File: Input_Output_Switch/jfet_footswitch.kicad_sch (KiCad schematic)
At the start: 48 parts, among them Q1 MMBF4393LT1G, Q2 PZT2222A, Q3 MMBF4393LT1G, Q4 PZT2222A, SW1 SW_Push, U2 TL072

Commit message: Final version 1.0 ordered
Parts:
- removed Q2, Q4: PZT2222A, Package_TO_SOT_SMD:SOT-23, symbol Transistor_BJT:PZT2222A
- added Q2, Q4: 2N4401D75ZCT-ND, Package_TO_SOT_THT:TO-92_Inline_Wide, symbol Device:Q_NPN_EBC
- C10, C11, C12, C13, C14, C15, C16: footprint Capacitor_SMD:C_0805_2012Metric -> Capacitor_SMD:C_0603_1608Metric_Pad1.08x0.95mm_HandSolder
- TP1, TP13, TP14, TP2, TP3, TP6, TPG3, TPG4: now left out of the parts list
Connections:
- net GNDA: now also Q2.1 (E), Q4.1 (E)
- net at C12.2, C14.1, R16.1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: now also Q4.2 (B)
- net at C15.1, R18.1, R20.1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: now also Q4.3 (C)
- net at C13.2, C15.2, R15.2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: now also Q2.2 (B)
- net at C12.1, D4.1 (K), R13.1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: now also Q2.3 (C)
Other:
- title: (none) -> EQ8-Main-Board

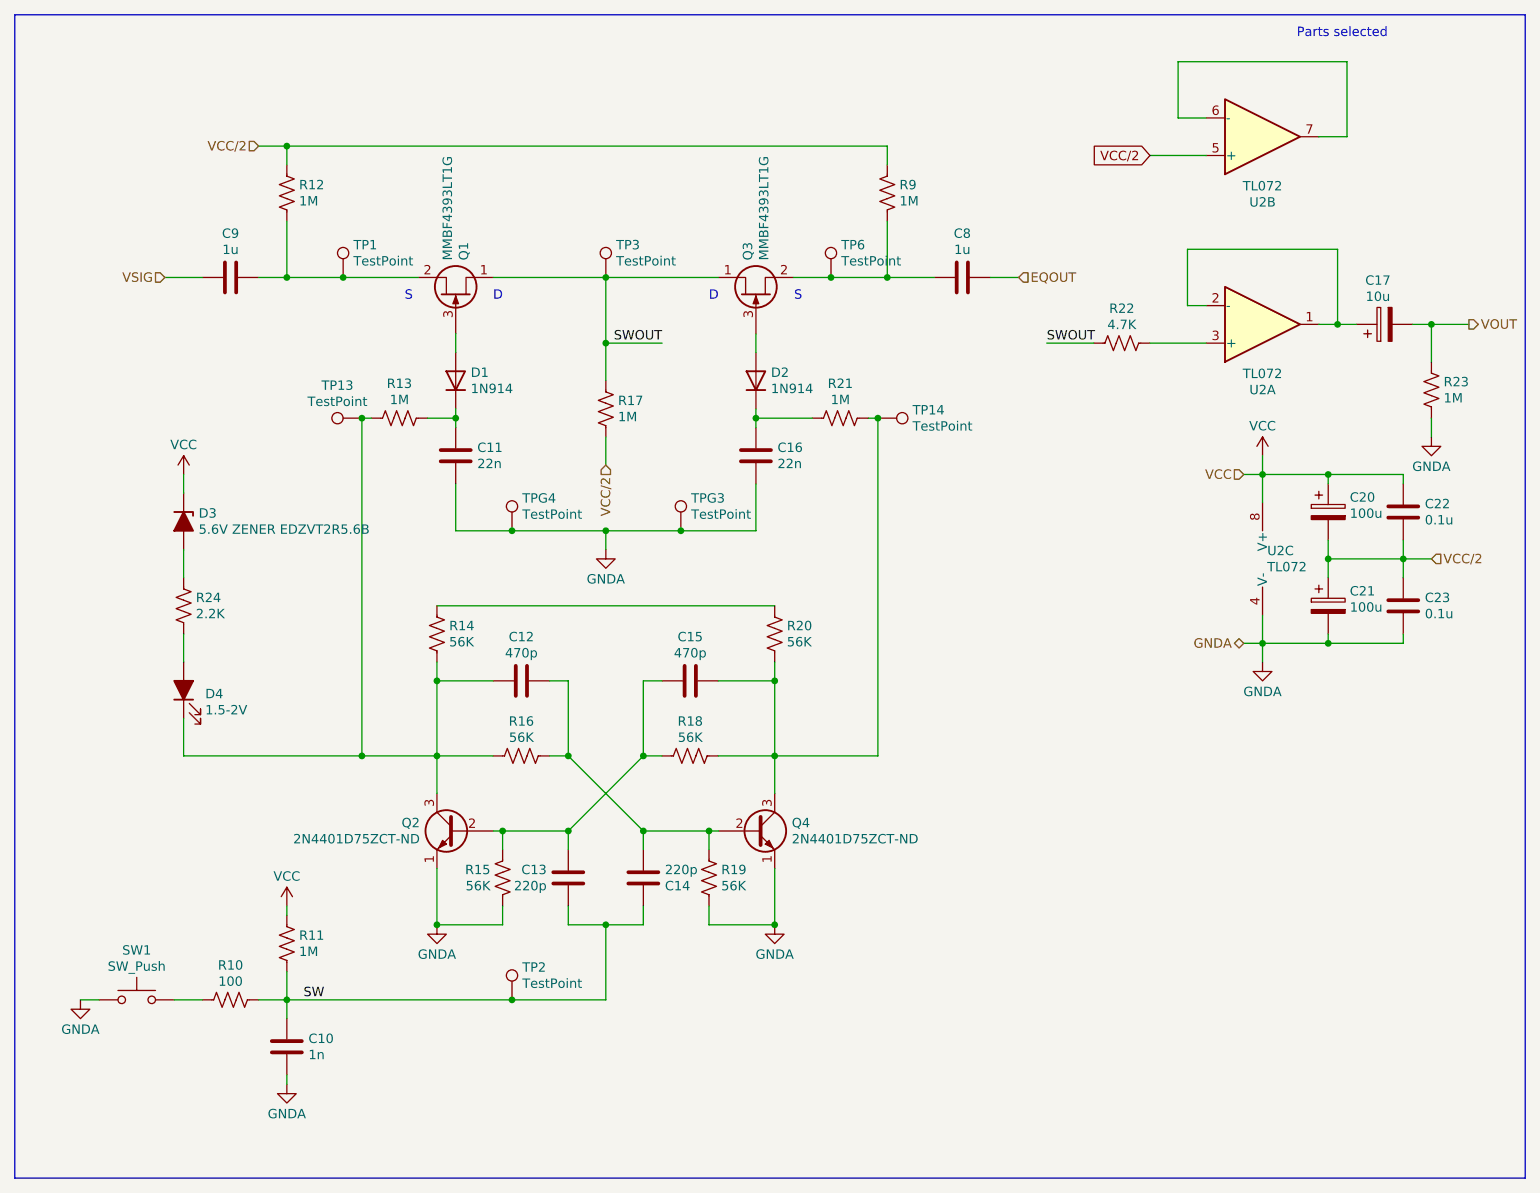
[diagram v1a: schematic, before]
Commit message: Fix bypass resistor, add missing Vcc. Move to Kicad-9
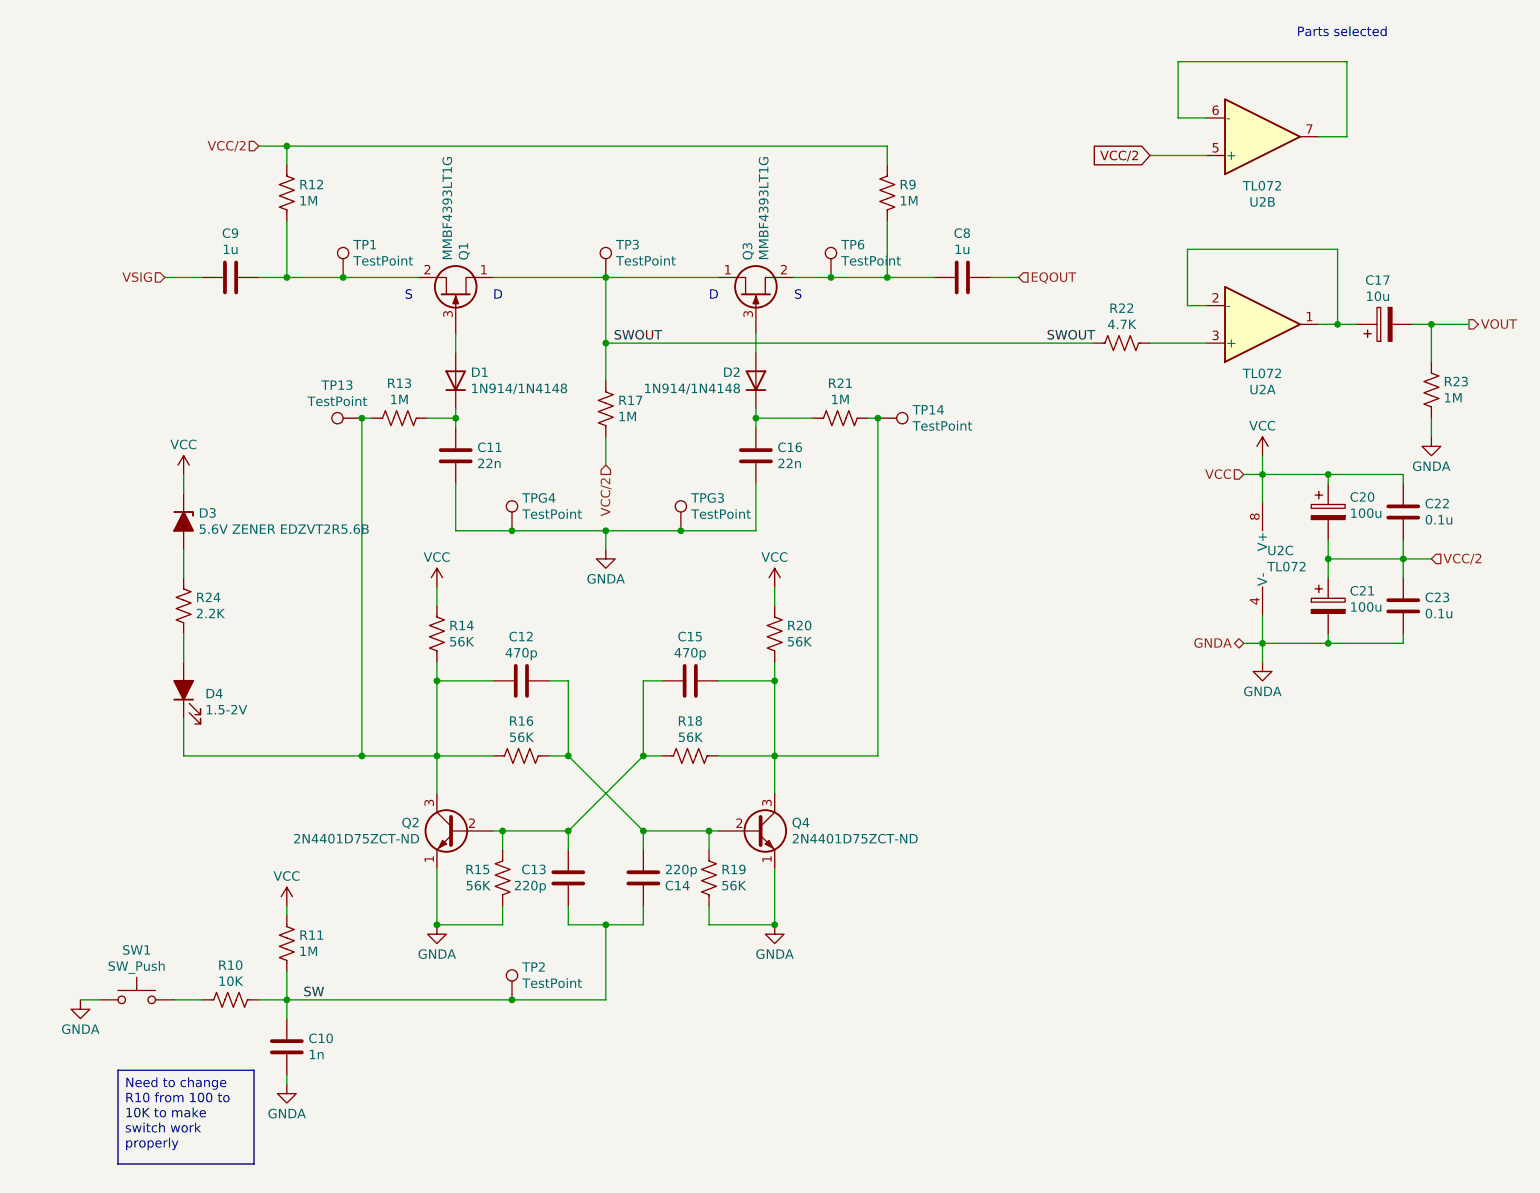
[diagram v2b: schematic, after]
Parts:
- D1, D2: value 1N914 -> 1N914/1N4148
- R10: value 100 -> 10K
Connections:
- net VCC: now also R14.2, R20.2
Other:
- moved on the sheet: D2
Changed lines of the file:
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@@
 (kicad_sch
-	(version 20231120)
+	(version 20250114)
 	(generator "eeschema")
-	(generator_version "8.0")
+	(generator_version "9.0")
 	(paper "A4")
 	(title_block
 		(title "EQ8-Main-Board")
-		(date "2024-11-23")
-		(rev "1.0")
+		(date "2025-07-25")
+		(rev "v1.1")
+	)
+	(text "D"
+		(exclude_from_sim no)
+		(at 125.095 52.07 0)
+		(effects
+			(font
+				(size 1.27 1.27)
+			)
+		)
+	)
+	(text "D"
+		(exclude_from_sim no)
+		(at 154.305 52.07 0)
+		(effects
+			(font
+				(size 1.27 1.27)
+			)
+		)
+	)
+	(text "S"
+		(exclude_from_sim no)
+		(at 165.735 52.07 0)
+		(effects
+			(font
+				(size 1.27 1.27)
+			)
+		)
+	)
+	(text "Parts selected"
+		(exclude_from_sim no)
+		(at 239.395 16.51 0)
+		(effects
+			(font
+				(size 1.27 1.27)
+			)
+		)
+	)
+	(text "S"
+		(exclude_from_sim no)
+		(at 113.03 52.07 0)
+		(effects
+			(font
+				(size 1.27 1.27)
+			)
+		)
+	)
+	(text_box "Need to change R10 from 100 to 10K to make switch work properly"
+		(exclude_from_sim no)
+		(at 73.66 156.845 0)
+		(size 18.415 12.7)
+		(margins 0.9525 0.9525 0.9525 0.9525)
+		(stroke
+			(width 0)
+			(type default)
+		)
+		(fill
+			(type none)
+		)
+		(effects
+			(font
+				(size 1.27 1.27)
+			)
+			(justify left top)
+		)
 	)
 	(junction
@@
 	(wire
 		(pts
-			(xy 116.84 93.98) (xy 162.56 93.98)
-		)
-		(stroke
-			(width 0)
-			(type default)
-		)
-	)
-	(wire
-		(pts
 			(xy 119.38 57.15) (xy 119.38 59.69)
 		)
@@
 	(wire
 		(pts
-			(xy 199.39 58.42) (xy 205.74 58.42)
-		)
-		(stroke
-			(width 0)
-			(type default)
-		)
-	)
-	(wire
-		(pts
 			(xy 81.28 147.32) (xy 85.09 147.32)
 		)
@@
 	(wire
 		(pts
-			(xy 139.7 58.42) (xy 147.32 58.42)
+			(xy 139.7 58.42) (xy 205.74 58.42)
 		)
 		(stroke
@@
 	(wire
 		(pts
+			(xy 162.56 91.44) (xy 162.56 93.98)
+		)
+		(stroke
+			(width 0)
+			(type default)
+		)
+	)
+	(wire
+		(pts
 			(xy 96.52 41.91) (xy 96.52 49.53)
 		)
@@
 	(wire
 		(pts
-			(xy 139.7 83.82) (xy 149.86 83.82)
+			(xy 116.84 91.44) (xy 116.84 93.98)
 		)
 		(stroke
@@
 	(wire
 		(pts
-			(xy 162.56 101.6) (xy 162.56 104.14)
+			(xy 139.7 83.82) (xy 149.86 83.82)
 		)
 		(stroke
@@
 	(wire
 		(pts
-			(xy 160.02 83.82) (xy 160.02 77.47)
+			(xy 162.56 101.6) (xy 162.56 104.14)
 		)
 		(stroke
@@
 		)
 	)
-	(rectangle
-		(start 59.69 13.97)
-		(end 264.16 171.45)
+	(wire
+		(pts
+			(xy 160.02 83.82) (xy 160.02 77.47)
+		)
 		(stroke
 			(width 0)
 			(type default)
 		)
-		(fill
-			(type none)
-		)
-	)
-	(text "D"
-		(exclude_from_sim no)
-		(at 125.095 52.07 0)
-		(effects
-			(font
-				(size 1.27 1.27)
-			)
-		)
-	)
-	(text "D"
-		(exclude_from_sim no)
-		(at 154.305 52.07 0)
-		(effects
-			(font
-				(size 1.27 1.27)
-			)
-		)
-	)
-	(text "S"
-		(exclude_from_sim no)
-		(at 165.735 52.07 0)
-		(effects
-			(font
-				(size 1.27 1.27)
-			)
-		)
-	)
-	(text "Parts selected"
-		(exclude_from_sim no)
-		(at 239.395 16.51 0)
-		(effects
-			(font
-				(size 1.27 1.27)
-			)
-		)
-	)
-	(text "S"
-		(exclude_from_sim no)
-		(at 113.03 52.07 0)
-		(effects
-			(font
-				(size 1.27 1.27)
-			)
-		)
 	)
 	(label "SW"
 		(at 101.6 147.32 180)
-		(fields_autoplaced yes)
 		(effects
 			(font
@@
 	(label "SWOUT"
 		(at 147.32 58.42 180)
-		(fields_autoplaced yes)
 		(effects
 			(font
@@
 	(label "SWOUT"
 		(at 199.39 58.42 0)
-		(fields_autoplaced yes)
 		(effects
 			(font
@@
 		(shape input)
 		(at 139.7 74.93 270)
-		(fields_autoplaced yes)
 		(effects
 			(font
@@
 		(shape input)
 		(at 80.01 49.53 180)
-		(fields_autoplaced yes)
 		(effects
 			(font
@@
 		(shape input)
 		(at 226.06 76.2 180)
-		(fields_autoplaced yes)
 		(effects
 			(font
@@
 		(shape input)
 		(at 195.58 49.53 0)
-		(fields_autoplaced yes)
 		(effects
 			(font
@@
 		(shape output)
 		(at 256.54 55.88 0)
-		(fields_autoplaced yes)
 		(effects
 			(font
@@
 		(shape input)
 		(at 92.71 31.75 180)
-		(fields_autoplaced yes)
 		(effects
 			(font
@@
 		(shape bidirectional)
 		(at 226.06 99.06 180)
-		(fields_autoplaced yes)
 		(effects
 			(font
@@
 		(shape input)
 		(at 251.46 87.63 0)
-		(fields_autoplaced yes)
 		(effects
 			(font
@@
 		(fields_autoplaced yes)
 		(property "Reference" "R10"
-			(at 88.9 142.6417 90)
+			(at 88.9 142.6716 90)
 			(effects
 				(font
@@
 			)
 		)
-		(property "Value" "100"
-			(at 88.9 144.8292 90)
+		(property "Value" "10K"
+			(at 88.9 144.8392 90)
 			(effects
 				(font
@@
 	)
 	(symbol
+		(lib_id "power:VCC")
+		(at 116.84 91.44 0)
+		(unit 1)
+		(exclude_from_sim no)
+		(in_bom yes)
+		(on_board yes)
+		(dnp no)
+		(fields_autoplaced yes)
+		(property "Reference" "#PWR021"
+			(at 116.84 95.25 0)
+			(effects
+				(font
+					(size 1.27 1.27)
+				)
+				(hide yes)
+			)
+		)
+		(property "Value" "VCC"
+			(at 116.84 87.4253 0)
+			(effects
+				(font
+					(size 1.27 1.27)
+				)
+			)
+		)
+		(property "Footprint" ""
+			(at 116.84 91.44 0)
+			(effects
+				(font
+					(size 1.27 1.27)
+				)
+				(hide yes)
+			)
+		)
+		(property "Datasheet" ""
+			(at 116.84 91.44 0)
+			(effects
+				(font
+					(size 1.27 1.27)
+				)
+				(hide yes)
+			)
+		)
+		(property "Description" "Power symbol creates a global label with name \"VCC\""
+			(at 116.84 91.44 0)
+			(effects
+				(font
+					(size 1.27 1.27)
+				)
+				(hide yes)
+			)
+		)
+		(pin "1"
+		)
+		(instances
+			(project "Input_Output_Switch"
+				(path "/94a0f742-9aa3-4c6d-b577-3626080b87f8/c0c47698-2709-45c1-94fb-a230c1b8fcb0"
+					(reference "#PWR021")
+					(unit 1)
+				)
+			)
+		)
+	)
+	(symbol
 		(lib_id "Device:C_Polarized")
 		(at 237.49 81.28 0)
@@
 	)
 	(symbol
+		(lib_id "power:VCC")
+		(at 162.56 91.44 0)
+		(unit 1)
+		(exclude_from_sim no)
+		(in_bom yes)
+		(on_board yes)
+		(dnp no)
+		(fields_autoplaced yes)
+		(property "Reference" "#PWR024"
+			(at 162.56 95.25 0)
+			(effects
+				(font
+					(size 1.27 1.27)
+				)
+				(hide yes)
+			)
+		)
+		(property "Value" "VCC"
+			(at 162.56 87.4253 0)
+			(effects
+				(font
+					(size 1.27 1.27)
+				)
+			)
+		)
+		(property "Footprint" ""
+			(at 162.56 91.44 0)
+			(effects
+				(font
+					(size 1.27 1.27)
+				)
+				(hide yes)
+			)
+		)
+		(property "Datasheet" ""
+			(at 162.56 91.44 0)
+			(effects
+				(font
+					(size 1.27 1.27)
+				)
+				(hide yes)
+			)
+		)
+		(property "Description" "Power symbol creates a global label with name \"VCC\""
+			(at 162.56 91.44 0)
+			(effects
+				(font
+					(size 1.27 1.27)
+				)
+				(hide yes)
+			)
+		)
+		(pin "1"
+		)
+		(instances
+			(project "Input_Output_Switch"
+				(path "/94a0f742-9aa3-4c6d-b577-3626080b87f8/c0c47698-2709-45c1-94fb-a230c1b8fcb0"
+					(reference "#PWR024")
+					(unit 1)
+				)
+			)
+		)
+	)
+	(symbol
 		(lib_id "Connector:TestPoint")
 		(at 176.53 68.58 270)
@@
 	(symbol
 		(lib_id "Diode:1N914")
-		(at 160.02 63.5 90)
+		(at 160.02 63.5 270)
+		(mirror x)
 		(unit 1)
 		(exclude_from_sim no)
@@
 		(on_board yes)
 		(dnp no)
-		(fields_autoplaced yes)
 		(property "Reference" "D2"
-			(at 162.052 62.4062 90)
+			(at 157.988 62.4062 90)
 			(effects
 				(font
@@
 			)
 		)
-		(property "Value" "1N914"
-			(at 162.052 64.5937 90)
+		(property "Value" "1N914/1N4148"
+			(at 157.988 64.5937 90)
 			(effects
 				(font
@@
 		)
 		(property "Footprint" "Diode_THT:D_DO-35_SOD27_P2.54mm_Vertical_AnodeUp"
-			(at 164.465 63.5 0)
+			(at 155.575 63.5 0)
 			(effects
 				(font
@@
 			)
 		)
-		(property "Value" "1N914"
+		(property "Value" "1N914/1N4148"
 			(at 121.412 64.5937 90)
 			(effects
